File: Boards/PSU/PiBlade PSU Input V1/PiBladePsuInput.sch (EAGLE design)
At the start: 35 parts, among them J1 CONN_20X2NOSILK, Q1 220mA/50V/3.5Ω, Q2 220mA/50V/3.5Ω, Q3 220mA/50V/3.5Ω, U1 INA219AIDCNRSOIC, U2 R-78E5.0-1.0, U4 Tiny85-20-SMT

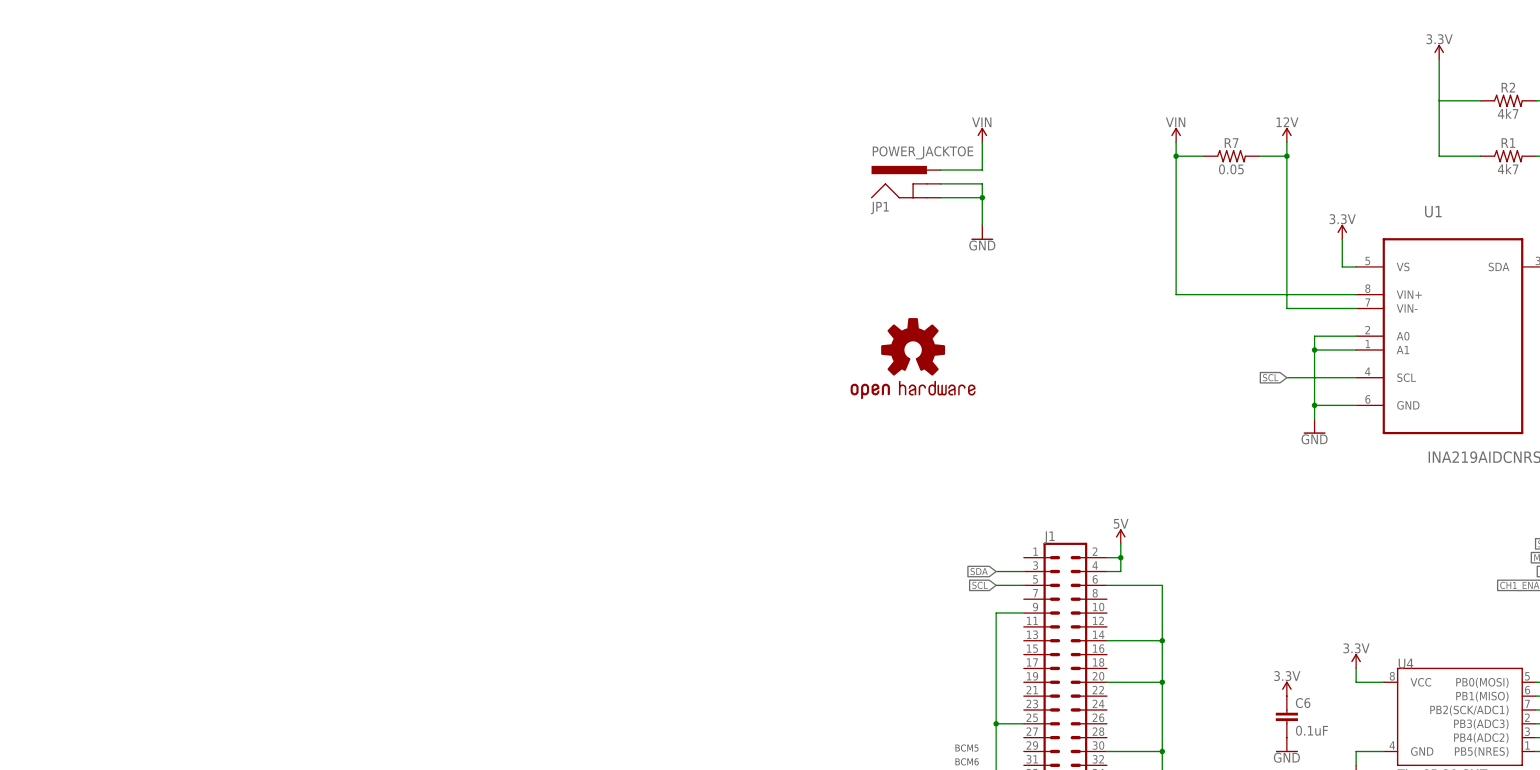
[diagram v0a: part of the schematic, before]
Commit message: Update PSU input board: * Added LEDs. * Moved DC Jack input to a lower position to align with the USB board better.
Updated DirtyPCBs
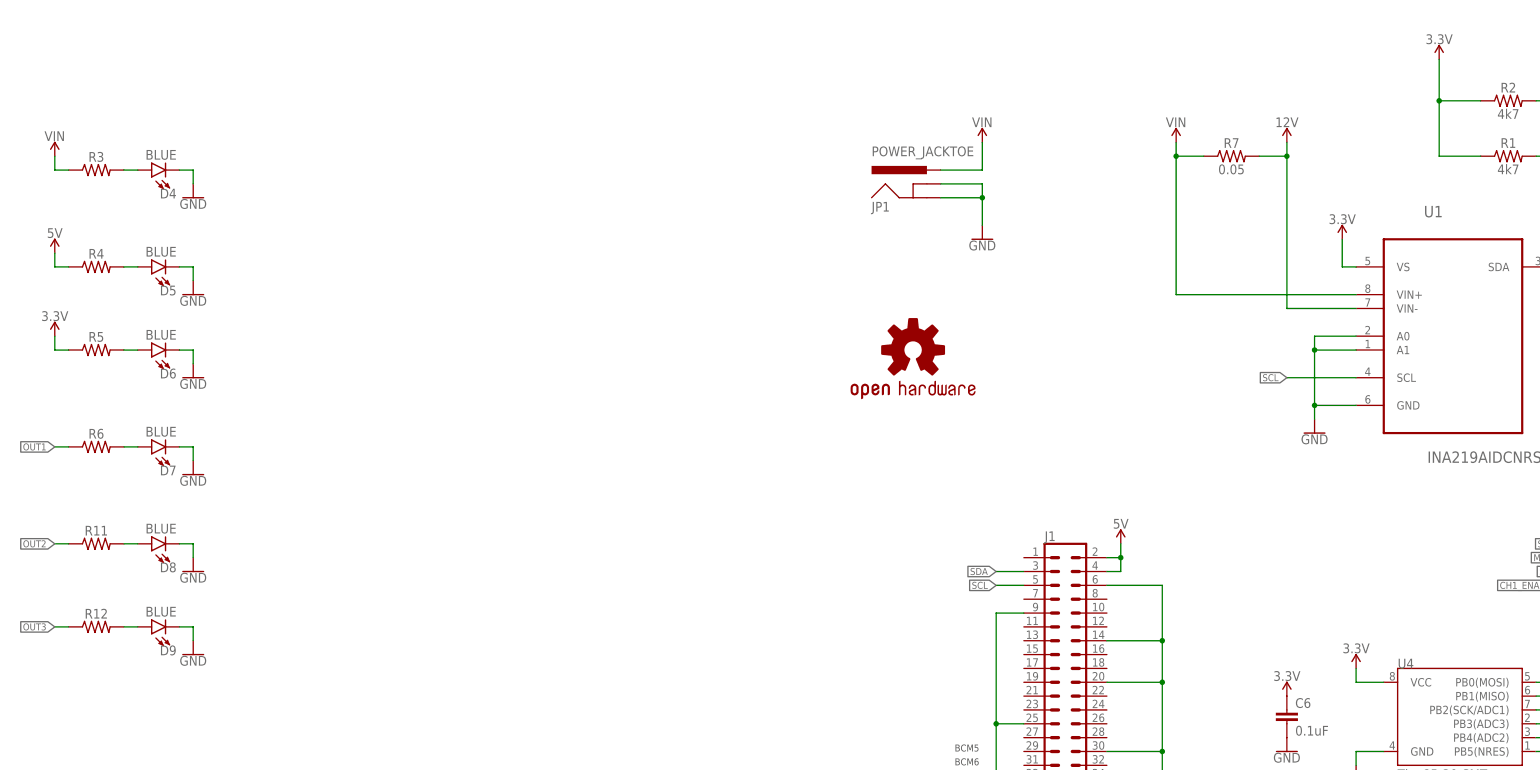
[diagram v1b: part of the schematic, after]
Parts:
- added D4, D5, D6, D7, D8, D9: BLUE, SparkFun-LED:LED-BLUE1206
- added R11, R12, R3, R4, R5, R6: (no value), SparkFun-Resistors:RESISTOR0805
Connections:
- new net N$1: D4.A, R3.2
- new net N$2: D6.A, R5.2
- new net N$3: D7.A, R6.2
- new net N$4: D5.A, R4.2
- new net N$5: D8.A, R11.2
- new net N$6: D9.A, R12.2
- net 3.3V: now also R5.1
- net 5V: now also R4.1
- net GND: now also D4.C, D5.C, D6.C, D7.C, D8.C, D9.C
- net OUT1: now also R6.1
- net OUT2: now also R11.1
- net OUT3: now also R12.1
- net VIN: now also R3.1
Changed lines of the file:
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@@
 <part name="R2" library="SparkFun-Resistors" deviceset="RESISTOR" device="0805" value="4k7"/>
 <part name="SUPPLY12" library="SparkFun-PowerSymbols" deviceset="3.3V" device=""/>
+<part name="R3" library="SparkFun-Resistors" deviceset="RESISTOR" device="0805" value=" "/>
+<part name="D4" library="SparkFun-LED" deviceset="LED-BLUE" device="1206" value="BLUE"/>
+<part name="GND27" library="SparkFun-PowerSymbols" deviceset="GND" device=""/>
+<part name="SUPPLY18" library="SparkFun-PowerSymbols" deviceset="VIN" device=""/>
+<part name="R4" library="SparkFun-Resistors" deviceset="RESISTOR" device="0805" value=" "/>
+<part name="D5" library="SparkFun-LED" deviceset="LED-BLUE" device="1206" value="BLUE"/>
+<part name="GND28" library="SparkFun-PowerSymbols" deviceset="GND" device=""/>
+<part name="R5" library="SparkFun-Resistors" deviceset="RESISTOR" device="0805" value=" "/>
+<part name="D6" library="SparkFun-LED" deviceset="LED-BLUE" device="1206" value="BLUE"/>
+<part name="GND29" library="SparkFun-PowerSymbols" deviceset="GND" device=""/>
+<part name="R6" library="SparkFun-Resistors" deviceset="RESISTOR" device="0805" value=" "/>
+<part name="D7" library="SparkFun-LED" deviceset="LED-BLUE" device="1206" value="BLUE"/>
+<part name="GND30" library="SparkFun-PowerSymbols" deviceset="GND" device=""/>
+<part name="R11" library="SparkFun-Resistors" deviceset="RESISTOR" device="0805" value=" "/>
+<part name="D8" library="SparkFun-LED" deviceset="LED-BLUE" device="1206" value="BLUE"/>
+<part name="GND31" library="SparkFun-PowerSymbols" deviceset="GND" device=""/>
+<part name="R12" library="SparkFun-Resistors" deviceset="RESISTOR" device="0805" value=" "/>
+<part name="D9" library="SparkFun-LED" deviceset="LED-BLUE" device="1206" value="BLUE"/>
+<part name="GND32" library="SparkFun-PowerSymbols" deviceset="GND" device=""/>
+<part name="SUPPLY24" library="SparkFun-PowerSymbols" deviceset="5V" device=""/>
+<part name="SUPPLY25" library="SparkFun-PowerSymbols" deviceset="3.3V" device=""/>
 </parts>
 <sheets>
@@
 <instance part="R2" gate="G$1" x="127" y="35.56"/>
 <instance part="SUPPLY12" gate="G$1" x="114.3" y="43.18"/>
+<instance part="R3" gate="G$1" x="-132.08" y="22.86"/>
+<instance part="D4" gate="G$1" x="-121.92" y="22.86" rot="R90"/>
+<instance part="GND27" gate="1" x="-114.3" y="17.78"/>
+<instance part="SUPPLY18" gate="G$1" x="-139.7" y="25.4"/>
+<instance part="R4" gate="G$1" x="-132.08" y="5.08"/>
+<instance part="D5" gate="G$1" x="-121.92" y="5.08" rot="R90"/>
+<instance part="GND28" gate="1" x="-114.3" y="0"/>
+<instance part="R5" gate="G$1" x="-132.08" y="-10.16"/>
+<instance part="D6" gate="G$1" x="-121.92" y="-10.16" rot="R90"/>
+<instance part="GND29" gate="1" x="-114.3" y="-15.24"/>
+<instance part="R6" gate="G$1" x="-132.08" y="-27.94"/>
+<instance part="D7" gate="G$1" x="-121.92" y="-27.94" rot="R90"/>
+<instance part="GND30" gate="1" x="-114.3" y="-33.02"/>
+<instance part="R11" gate="G$1" x="-132.08" y="-45.72"/>
+<instance part="D8" gate="G$1" x="-121.92" y="-45.72" rot="R90"/>
+<instance part="GND31" gate="1" x="-114.3" y="-50.8"/>
+<instance part="R12" gate="G$1" x="-132.08" y="-60.96"/>
+<instance part="D9" gate="G$1" x="-121.92" y="-60.96" rot="R90"/>
+<instance part="GND32" gate="1" x="-114.3" y="-66.04"/>
+<instance part="SUPPLY24" gate="G$1" x="-139.7" y="7.62"/>
+<instance part="SUPPLY25" gate="G$1" x="-139.7" y="-7.62"/>
 </instances>
 <busses>
@@
 <junction x="66.04" y="25.4"/>
 <pinref part="R7" gate="G$1" pin="1"/>
+</segment>
+<segment>
+<pinref part="R3" gate="G$1" pin="1"/>
+<wire x1="-137.16" y1="22.86" x2="-139.7" y2="22.86" width="0.1524" layer="91"/>
+<wire x1="-139.7" y1="22.86" x2="-139.7" y2="25.4" width="0.1524" layer="91"/>
+<pinref part="SUPPLY18" gate="G$1" pin="VIN"/>
 </segment>
 </net>
@@
 <pinref part="GND26" gate="1" pin="GND"/>
 </segment>
+<segment>
+<pinref part="D4" gate="G$1" pin="C"/>
+<wire x1="-116.84" y1="22.86" x2="-114.3" y2="22.86" width="0.1524" layer="91"/>
+<wire x1="-114.3" y1="22.86" x2="-114.3" y2="20.32" width="0.1524" layer="91"/>
+<pinref part="GND27" gate="1" pin="GND"/>
+</segment>
+<segment>
+<pinref part="D5" gate="G$1" pin="C"/>
+<wire x1="-116.84" y1="5.08" x2="-114.3" y2="5.08" width="0.1524" layer="91"/>
+<wire x1="-114.3" y1="5.08" x2="-114.3" y2="2.54" width="0.1524" layer="91"/>
+<pinref part="GND28" gate="1" pin="GND"/>
+</segment>
+<segment>
+<pinref part="D6" gate="G$1" pin="C"/>
+<wire x1="-116.84" y1="-10.16" x2="-114.3" y2="-10.16" width="0.1524" layer="91"/>
+<wire x1="-114.3" y1="-10.16" x2="-114.3" y2="-12.7" width="0.1524" layer="91"/>
+<pinref part="GND29" gate="1" pin="GND"/>
+</segment>
+<segment>
+<pinref part="D7" gate="G$1" pin="C"/>
+<wire x1="-116.84" y1="-27.94" x2="-114.3" y2="-27.94" width="0.1524" layer="91"/>
+<wire x1="-114.3" y1="-27.94" x2="-114.3" y2="-30.48" width="0.1524" layer="91"/>
+<pinref part="GND30" gate="1" pin="GND"/>
+</segment>
+<segment>
+<pinref part="D8" gate="G$1" pin="C"/>
+<wire x1="-116.84" y1="-45.72" x2="-114.3" y2="-45.72" width="0.1524" layer="91"/>
+<wire x1="-114.3" y1="-45.72" x2="-114.3" y2="-48.26" width="0.1524" layer="91"/>
+<pinref part="GND31" gate="1" pin="GND"/>
+</segment>
+<segment>
+<pinref part="D9" gate="G$1" pin="C"/>
+<wire x1="-116.84" y1="-60.96" x2="-114.3" y2="-60.96" width="0.1524" layer="91"/>
+<wire x1="-114.3" y1="-60.96" x2="-114.3" y2="-63.5" width="0.1524" layer="91"/>
+<pinref part="GND32" gate="1" pin="GND"/>
+</segment>
 </net>
 <net name="5V" class="0">
@@
 <junction x="55.88" y="-48.26"/>
 </segment>
+<segment>
+<pinref part="R4" gate="G$1" pin="1"/>
+<pinref part="SUPPLY24" gate="G$1" pin="5V"/>
+<wire x1="-137.16" y1="5.08" x2="-139.7" y2="5.08" width="0.1524" layer="91"/>
+<wire x1="-139.7" y1="5.08" x2="-139.7" y2="7.62" width="0.1524" layer="91"/>
+</segment>
 </net>
 <net name="12V" class="0">
@@
 <label x="335.28" y="22.86" size="1.27" layer="95" rot="R180" xref="yes"/>
 </segment>
+<segment>
+<pinref part="R12" gate="G$1" pin="1"/>
+<wire x1="-137.16" y1="-60.96" x2="-139.7" y2="-60.96" width="0.1524" layer="91"/>
+<label x="-139.7" y="-60.96" size="1.27" layer="95" rot="R180" xref="yes"/>
+</segment>
 </net>
 <net name="OUT1" class="0">
@@
 <label x="241.3" y="22.86" size="1.27" layer="95" rot="R180" xref="yes"/>
 </segment>
+<segment>
+<pinref part="R6" gate="G$1" pin="1"/>
+<wire x1="-137.16" y1="-27.94" x2="-139.7" y2="-27.94" width="0.1524" layer="91"/>
+<label x="-139.7" y="-27.94" size="1.27" layer="95" rot="R180" xref="yes"/>
+</segment>
 </net>
 <net name="OUT2" class="0">
@@
 <wire x1="289.56" y1="22.86" x2="287.02" y2="22.86" width="0.1524" layer="91"/>
 <label x="287.02" y="22.86" size="1.27" layer="95" rot="R180" xref="yes"/>
+</segment>
+<segment>
+<pinref part="R11" gate="G$1" pin="1"/>
+<wire x1="-137.16" y1="-45.72" x2="-139.7" y2="-45.72" width="0.1524" layer="91"/>
+<label x="-139.7" y="-45.72" size="1.27" layer="95" rot="R180" xref="yes"/>
 </segment>
 </net>
@@
 <wire x1="121.92" y1="35.56" x2="114.3" y2="35.56" width="0.1524" layer="91"/>
 <pinref part="SUPPLY12" gate="G$1" pin="3.3V"/>
+<junction x="114.3" y="35.56"/>
+</segment>
+<segment>
+<pinref part="R5" gate="G$1" pin="1"/>
+<pinref part="SUPPLY25" gate="G$1" pin="3.3V"/>
+<wire x1="-137.16" y1="-10.16" x2="-139.7" y2="-10.16" width="0.1524" layer="91"/>
+<wire x1="-139.7" y1="-10.16" x2="-139.7" y2="-7.62" width="0.1524" layer="91"/>
 </segment>
 </net>
@@
 </segment>
 </net>
+<net name="N$1" class="0">
+<segment>
+<pinref part="R3" gate="G$1" pin="2"/>
+<wire x1="-127" y1="22.86" x2="-124.46" y2="22.86" width="0.1524" layer="91"/>
+<pinref part="D4" gate="G$1" pin="A"/>
+</segment>
+</net>
+<net name="N$4" class="0">
+<segment>
+<pinref part="R4" gate="G$1" pin="2"/>
+<wire x1="-127" y1="5.08" x2="-124.46" y2="5.08" width="0.1524" layer="91"/>
+<pinref part="D5" gate="G$1" pin="A"/>
+</segment>
+</net>
+<net name="N$2" class="0">
+<segment>
+<pinref part="R5" gate="G$1" pin="2"/>
+<wire x1="-127" y1="-10.16" x2="-124.46" y2="-10.16" width="0.1524" layer="91"/>
+<pinref part="D6" gate="G$1" pin="A"/>
+</segment>
+</net>
+<net name="N$3" class="0">
+<segment>
+<pinref part="R6" gate="G$1" pin="2"/>
+<wire x1="-127" y1="-27.94" x2="-124.46" y2="-27.94" width="0.1524" layer="91"/>
+<pinref part="D7" gate="G$1" pin="A"/>
+</segment>
+</net>
+<net name="N$5" class="0">
+<segment>
+<pinref part="R11" gate="G$1" pin="2"/>
+<wire x1="-127" y1="-45.72" x2="-124.46" y2="-45.72" width="0.1524" layer="91"/>
+<pinref part="D8" gate="G$1" pin="A"/>
+</segment>
+</net>
+<net name="N$6" class="0">
+<segment>
+<pinref part="R12" gate="G$1" pin="2"/>
+<wire x1="-127" y1="-60.96" x2="-124.46" y2="-60.96" width="0.1524" layer="91"/>
+<pinref part="D9" gate="G$1" pin="A"/>
+</segment>
+</net>
